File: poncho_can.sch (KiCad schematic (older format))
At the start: 37 parts, among them J10 GS2, J101 DB9_Male_MountingHoles, J102 DB9_Male_MountingHoles, J103 GS2, J104 GS2, J105 GS2, J106 GS2, J7 GS2, J8 GS2, J9 GS2, U101 TJA1051T, U102 TJA1051T

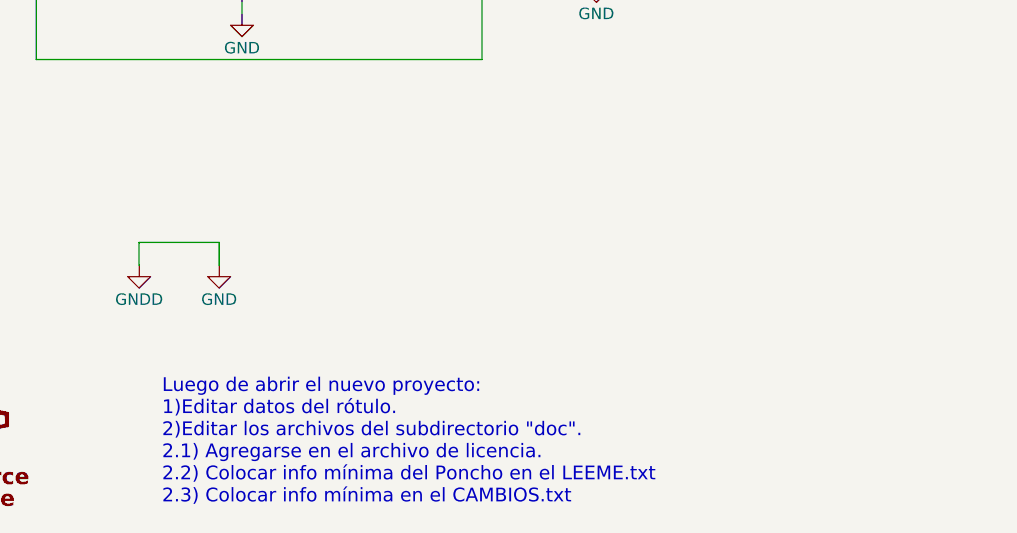
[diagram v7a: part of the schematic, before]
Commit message: Agrego documentacion y aplica cambios sugeridos en la revision
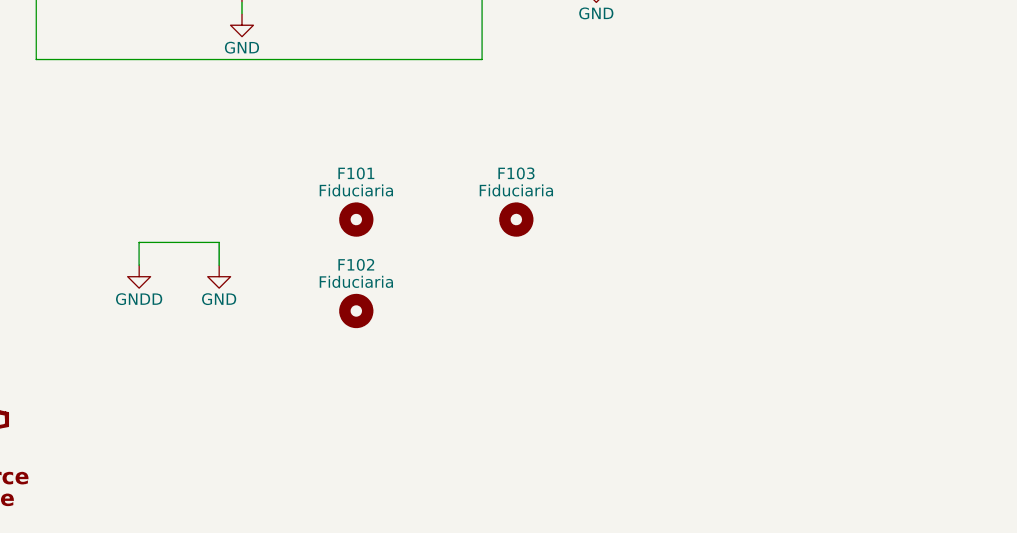
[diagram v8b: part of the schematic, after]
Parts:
- added F101, F102, F103: Fiduciaria, Fiducials:Fiducial_1mm_Dia_2.54mm_Outer_CopperBottom, symbol Mounting_Hole
- D101: footprint TO_SOT_Packages_SMD:SOT-23 -> TO_SOT_Packages_SMD:SOT-23W_Handsoldering
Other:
- note removed: "Luego de abrir el nuevo proyecto:\n1)Editar datos del rótulo.\n2)Editar los archivos del subdirectorio "doc".\n2.1) Agregarse en el archivo de licencia.\n2.2) Colocar info mínima del Poncho en el LEEME.txt\n2.3) Colocar info mínima en el CAMBIOS.txt"
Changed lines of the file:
@@
 	-1   0    0    -1
 $EndComp
-Text Notes 4200 7450 0    60   ~ 0
-Luego de abrir el nuevo proyecto:\n1)Editar datos del rótulo.\n2)Editar los archivos del subdirectorio "doc".\n2.1) Agregarse en el archivo de licencia.\n2.2) Colocar info mínima del Poncho en el LEEME.txt\n2.3) Colocar info mínima en el CAMBIOS.txt
 $Comp
 L Conn_Poncho2P_2x_20x2 XA101
@@
 F 0 "D101" H 3300 2775 50  0000 C CNN
 F 1 "RSB27C2" H 3300 2700 50  0000 C CNN
-F 2 "TO_SOT_Packages_SMD:SOT-23" H 3150 2600 50  0001 C CNN
+F 2 "TO_SOT_Packages_SMD:SOT-23W_Handsoldering" H 3150 2600 50  0001 C CNN
 F 3 "" H 3150 2600 50  0001 C CNN
 	1    3300 2600
@@
 $EndComp
 $Comp
-L GND #PWR019
+L GND #PWR018
 U 1 1 5BB59E2B
 P 2700 4550
-F 0 "#PWR019" H 2700 4300 50  0001 C CNN
+F 0 "#PWR018" H 2700 4300 50  0001 C CNN
 F 1 "GND" H 2700 4400 50  0000 C CNN
 F 2 "" H 2700 4550 50  0000 C CNN
@@
 $EndComp
 $Comp
-L GND #PWR020
+L GND #PWR019
 U 1 1 5BB59E72
 P 4550 5300
-F 0 "#PWR020" H 4550 5050 50  0001 C CNN
+F 0 "#PWR019" H 4550 5050 50  0001 C CNN
 F 1 "GND" H 4550 5150 50  0000 C CNN
 F 2 "" H 4550 5300 50  0000 C CNN
@@
 $EndComp
 $Comp
-L GND #PWR021
+L GND #PWR020
 U 1 1 5BB59E78
 P 4800 3950
-F 0 "#PWR021" H 4800 3700 50  0001 C CNN
+F 0 "#PWR020" H 4800 3700 50  0001 C CNN
 F 1 "GND" H 4800 3800 50  0000 C CNN
 F 2 "" H 4800 3950 50  0000 C CNN
@@
 $EndComp
 $Comp
-L GND #PWR022
+L GND #PWR021
 U 1 1 5BB59E8D
 P 6650 4100
-F 0 "#PWR022" H 6650 3850 50  0001 C CNN
+F 0 "#PWR021" H 6650 3850 50  0001 C CNN
 F 1 "GND" H 6650 3950 50  0000 C CNN
 F 2 "" H 6650 4100 50  0000 C CNN
@@
 $EndComp
 $Comp
-L GND #PWR023
+L GND #PWR022
 U 1 1 5BB59EA3
 P 3000 4650
-F 0 "#PWR023" H 3000 4400 50  0001 C CNN
+F 0 "#PWR022" H 3000 4400 50  0001 C CNN
 F 1 "GND" H 3000 4500 50  0000 C CNN
 F 2 "" H 3000 4650 50  0000 C CNN
@@
 $EndComp
 $Comp
-L +5V #PWR025
+L +5V #PWR023
 U 1 1 5BBC593B
 P 7150 1300
-F 0 "#PWR025" H 7150 1150 50  0001 C CNN
+F 0 "#PWR023" H 7150 1150 50  0001 C CNN
 F 1 "+5V" H 7150 1440 50  0000 C CNN
 F 2 "" H 7150 1300 50  0000 C CNN
@@
 NoConn ~ 2450 2300
 $Comp
-L GND #PWR026
+L GND #PWR024
 U 1 1 5BBC7C8B
 P 2150 3450
-F 0 "#PWR026" H 2150 3200 50  0001 C CNN
+F 0 "#PWR024" H 2150 3200 50  0001 C CNN
 F 1 "GND" H 2150 3300 50  0000 C CNN
 F 2 "" H 2150 3450 50  0000 C CNN
@@
 $EndComp
 $Comp
-L GND #PWR027
+L GND #PWR025
 U 1 1 5BBC7D83
 P 2150 5350
-F 0 "#PWR027" H 2150 5100 50  0001 C CNN
+F 0 "#PWR025" H 2150 5100 50  0001 C CNN
 F 1 "GND" H 2150 5200 50  0000 C CNN
 F 2 "" H 2150 5350 50  0000 C CNN
@@
 $EndComp
 $Comp
-L GNDD #PWR028
+L GNDD #PWR026
 U 1 1 5BBC9EE6
 P 4100 6400
-F 0 "#PWR028" H 4100 6150 50  0001 C CNN
+F 0 "#PWR026" H 4100 6150 50  0001 C CNN
 F 1 "GNDD" H 4100 6250 50  0000 C CNN
 F 2 "" H 4100 6400 50  0000 C CNN
@@
 $EndComp
 $Comp
-L GND #PWR029
+L GND #PWR027
 U 1 1 5BBC9F46
 P 4450 6400
-F 0 "#PWR029" H 4450 6150 50  0001 C CNN
+F 0 "#PWR027" H 4450 6150 50  0001 C CNN
 F 1 "GND" H 4450 6250 50  0000 C CNN
 F 2 "" H 4450 6400 50  0000 C CNN
@@
 CAN1-
 $Comp
-L PWR_FLAG #FLG030
+L PWR_FLAG #FLG028
 U 1 1 5BBD225C
 P 10000 1650
-F 0 "#FLG030" H 10000 1745 30  0001 C CNN
+F 0 "#FLG028" H 10000 1745 30  0001 C CNN
 F 1 "PWR_FLAG" H 10000 1830 30  0000 C CNN
 F 2 "" H 10000 1650 60  0000 C CNN
@@
 *3
 $Comp
-L +5VP #PWR?
+L +5VP #PWR029
 U 1 1 5BBD8B38
 P 7150 3350
-F 0 "#PWR?" H 7150 3440 20  0001 C CNN
+F 0 "#PWR029" H 7150 3440 20  0001 C CNN
 F 1 "+5VP" H 7150 3500 30  0000 C CNN
 F 2 "" H 7150 3350 60  0000 C CNN
@@
 $EndComp
 $Comp
-L +5VP #PWR?
+L +5VP #PWR030
 U 1 1 5BBD8CA5
 P 6100 3600
-F 0 "#PWR?" H 6100 3690 20  0001 C CNN
+F 0 "#PWR030" H 6100 3690 20  0001 C CNN
 F 1 "+5VP" H 6100 3750 30  0000 C CNN
 F 2 "" H 6100 3600 60  0000 C CNN
@@
 	-1   0    0    -1
 $EndComp
+$Comp
+L Mounting_Hole F101
+U 1 1 5BC954A9
+P 5050 6200
+F 0 "F101" H 5050 6400 50  0000 C CNN
+F 1 "Fiduciaria" H 5050 6325 50  0000 C CNN
+F 2 "Fiducials:Fiducial_1mm_Dia_2.54mm_Outer_CopperBottom" H 5050 6200 50  0001 C CNN
+F 3 "" H 5050 6200 50  0001 C CNN
+	1    5050 6200
+	1    0    0    -1
+$EndComp
+$Comp
+L Mounting_Hole F103
+U 1 1 5BC955C7
+P 5750 6200
+F 0 "F103" H 5750 6400 50  0000 C CNN
+F 1 "Fiduciaria" H 5750 6325 50  0000 C CNN
+F 2 "Fiducials:Fiducial_1mm_Dia_2.54mm_Outer_CopperBottom" H 5750 6200 50  0001 C CNN
+F 3 "" H 5750 6200 50  0001 C CNN
+	1    5750 6200
+	1    0    0    -1
+$EndComp
+$Comp
+L Mounting_Hole F102
+U 1 1 5BC9563C
+P 5050 6600
+F 0 "F102" H 5050 6800 50  0000 C CNN
+F 1 "Fiduciaria" H 5050 6725 50  0000 C CNN
+F 2 "Fiducials:Fiducial_1mm_Dia_2.54mm_Outer_CopperBottom" H 5050 6600 50  0001 C CNN
+F 3 "" H 5050 6600 50  0001 C CNN
+	1    5050 6600
+	1    0    0    -1
+$EndComp
 $EndSCHEMATC
